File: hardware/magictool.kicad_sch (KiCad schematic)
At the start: 3 parts, among them J1 magicTool I/O, J2 RUN

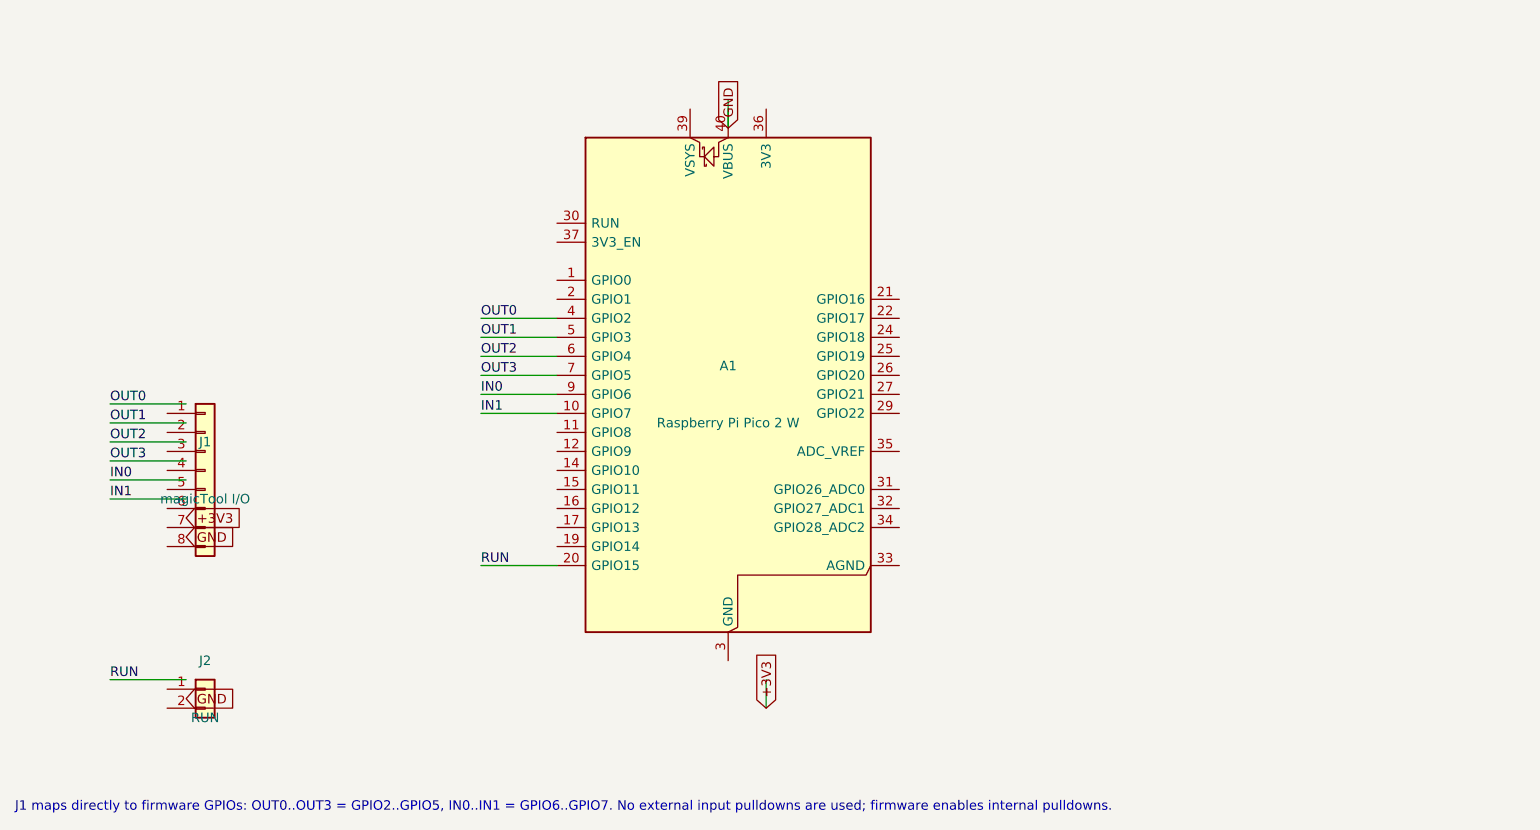
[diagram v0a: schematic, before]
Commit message: refactor(hardware): streamline schematic wiring and update labels
This commit enhances the Raspberry Pi Pico carrier schematic generation script by rerouting wires for improved readability, adjusting component positions for better alignment, and updating specific pin attributes to 'passive' where applicable. Additionally, it adds no-connect markers for unused Pico pins to prevent potential connection errors in the KiCad schematic. These changes aim to clarify signal routing and ensure consistency with standard schematic practices, thereby facilitating easier maintenance and modification of the design.
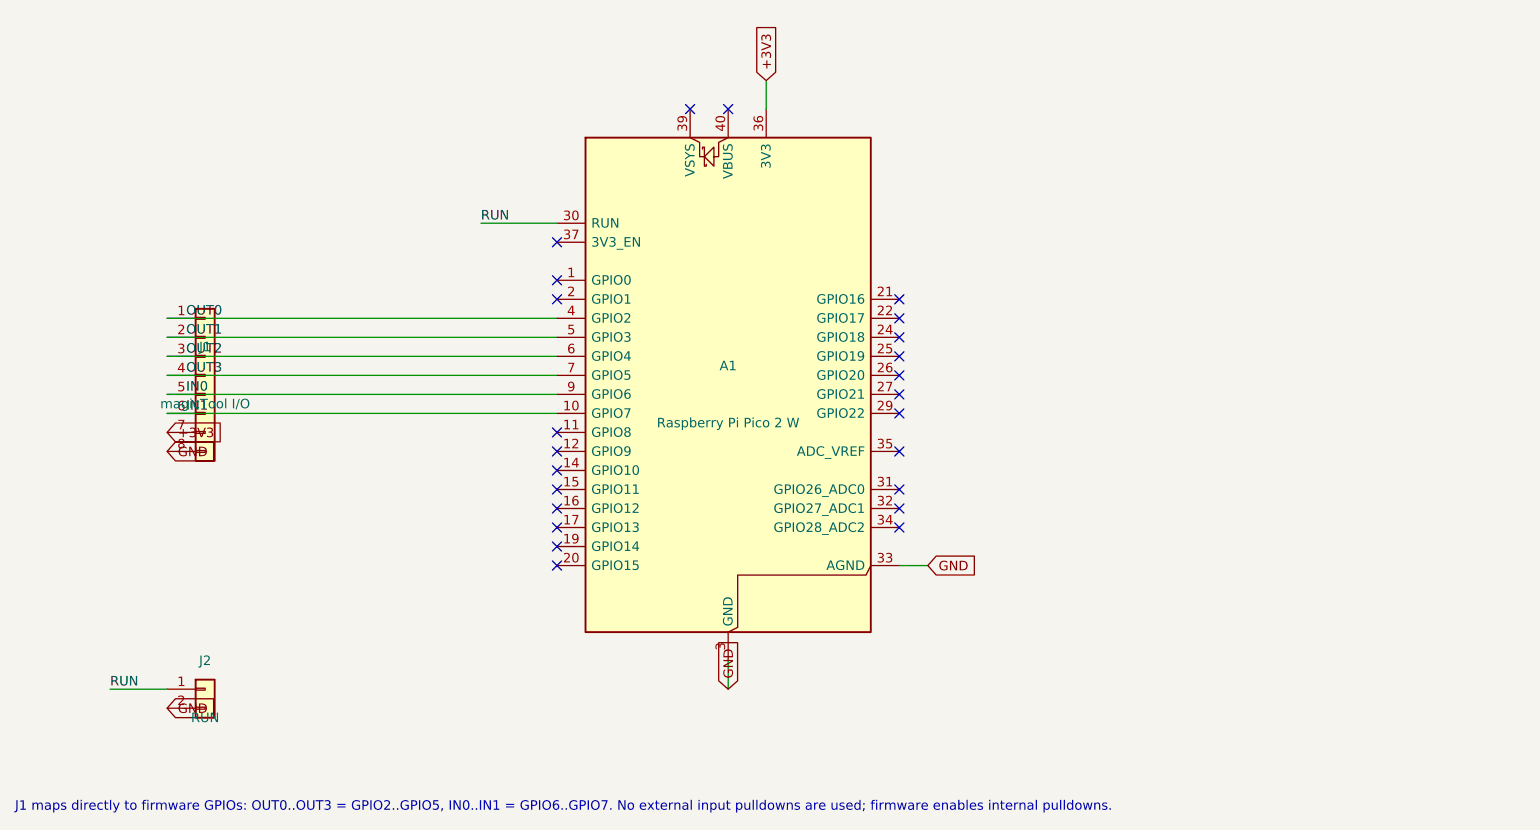
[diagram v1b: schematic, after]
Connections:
- net +3V3: now also A1.36 (3V3), J1.7 (Pin_7)
- net GND: now also A1.13 (GND), A1.18 (GND), A1.23 (GND), A1.28 (GND), A1.3 (GND), A1.33 (AGND), A1.38 (GND), A1.8 (GND), J1.8 (Pin_8), J2.2 (Pin_2)
- net IN0: now also J1.5 (Pin_5)
- net IN1: now also J1.6 (Pin_6)
- net OUT0: now also J1.1 (Pin_1)
- net OUT1: now also J1.2 (Pin_2)
- net OUT2: now also J1.3 (Pin_3)
- net OUT3: now also J1.4 (Pin_4)
- net RUN: now also A1.30 (RUN), J2.1 (Pin_1); no longer A1.20 (GPIO15)
- no-connect marks 0 -> 24
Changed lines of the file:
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@@
 	)
 	(wire
-		(pts (xy 97.79 78.74) (xy 87.63 78.74))
+		(pts (xy 45.72 78.74) (xy 97.79 78.74))
 		(stroke (width 0) (type default))
 	)
 	(label "OUT0"
-		(at 87.63 78.74 0)
-		(effects (font (size 1.27 1.27)) (justify left bottom))
-	)
-	(wire
-		(pts (xy 97.79 81.28) (xy 87.63 81.28))
+		(at 48.26 78.74 0)
+		(effects (font (size 1.27 1.27)) (justify left bottom))
+	)
+	(wire
+		(pts (xy 45.72 81.28) (xy 97.79 81.28))
 		(stroke (width 0) (type default))
 	)
 	(label "OUT1"
-		(at 87.63 81.28 0)
-		(effects (font (size 1.27 1.27)) (justify left bottom))
-	)
-	(wire
-		(pts (xy 97.79 83.82) (xy 87.63 83.82))
+		(at 48.26 81.28 0)
+		(effects (font (size 1.27 1.27)) (justify left bottom))
+	)
+	(wire
+		(pts (xy 45.72 83.82) (xy 97.79 83.82))
 		(stroke (width 0) (type default))
 	)
 	(label "OUT2"
-		(at 87.63 83.82 0)
-		(effects (font (size 1.27 1.27)) (justify left bottom))
-	)
-	(wire
-		(pts (xy 97.79 86.36) (xy 87.63 86.36))
+		(at 48.26 83.82 0)
+		(effects (font (size 1.27 1.27)) (justify left bottom))
+	)
+	(wire
+		(pts (xy 45.72 86.36) (xy 97.79 86.36))
 		(stroke (width 0) (type default))
 	)
 	(label "OUT3"
-		(at 87.63 86.36 0)
-		(effects (font (size 1.27 1.27)) (justify left bottom))
-	)
-	(wire
-		(pts (xy 97.79 88.9) (xy 87.63 88.9))
+		(at 48.26 86.36 0)
+		(effects (font (size 1.27 1.27)) (justify left bottom))
+	)
+	(wire
+		(pts (xy 45.72 88.9) (xy 97.79 88.9))
 		(stroke (width 0) (type default))
 	)
 	(label "IN0"
-		(at 87.63 88.9 0)
-		(effects (font (size 1.27 1.27)) (justify left bottom))
-	)
-	(wire
-		(pts (xy 97.79 91.44) (xy 87.63 91.44))
+		(at 48.26 88.9 0)
+		(effects (font (size 1.27 1.27)) (justify left bottom))
+	)
+	(wire
+		(pts (xy 45.72 91.44) (xy 97.79 91.44))
 		(stroke (width 0) (type default))
 	)
 	(label "IN1"
-		(at 87.63 91.44 0)
-		(effects (font (size 1.27 1.27)) (justify left bottom))
-	)
-	(wire
-		(pts (xy 48.26 90.17) (xy 38.1 90.17))
-		(stroke (width 0) (type default))
-	)
-	(label "OUT0"
-		(at 38.1 90.17 0)
-		(effects (font (size 1.27 1.27)) (justify left bottom))
-	)
-	(wire
-		(pts (xy 48.26 92.71) (xy 38.1 92.71))
-		(stroke (width 0) (type default))
-	)
-	(label "OUT1"
-		(at 38.1 92.71 0)
-		(effects (font (size 1.27 1.27)) (justify left bottom))
-	)
-	(wire
-		(pts (xy 48.26 95.25) (xy 38.1 95.25))
-		(stroke (width 0) (type default))
-	)
-	(label "OUT2"
-		(at 38.1 95.25 0)
-		(effects (font (size 1.27 1.27)) (justify left bottom))
-	)
-	(wire
-		(pts (xy 48.26 97.79) (xy 38.1 97.79))
-		(stroke (width 0) (type default))
-	)
-	(label "OUT3"
-		(at 38.1 97.79 0)
-		(effects (font (size 1.27 1.27)) (justify left bottom))
-	)
-	(wire
-		(pts (xy 48.26 100.33) (xy 38.1 100.33))
-		(stroke (width 0) (type default))
-	)
-	(label "IN0"
-		(at 38.1 100.33 0)
-		(effects (font (size 1.27 1.27)) (justify left bottom))
-	)
-	(wire
-		(pts (xy 48.26 102.87) (xy 38.1 102.87))
-		(stroke (width 0) (type default))
-	)
-	(label "IN1"
-		(at 38.1 102.87 0)
+		(at 48.26 91.44 0)
 		(effects (font (size 1.27 1.27)) (justify left bottom))
 	)
 	(global_label "+3V3"
 		(shape input)
-		(at 48.26 105.41 180)
-		(fields_autoplaced yes)
-		(effects (font (size 1.27 1.27)) (justify left))
-		(property "Intersheetrefs" "${INTERSHEET_REFS}" (at 48.26 105.41 0)
+		(at 45.72 93.98 180)
+		(fields_autoplaced yes)
+		(effects (font (size 1.27 1.27)) (justify left))
+		(property "Intersheetrefs" "${INTERSHEET_REFS}" (at 45.72 93.98 0)
 			(effects (font (size 1.27 1.27)) (hide yes))
 		)
@@
 	(global_label "GND"
 		(shape input)
-		(at 48.26 107.95 180)
-		(fields_autoplaced yes)
-		(effects (font (size 1.27 1.27)) (justify left))
-		(property "Intersheetrefs" "${INTERSHEET_REFS}" (at 48.26 107.95 0)
+		(at 45.72 96.52 180)
+		(fields_autoplaced yes)
+		(effects (font (size 1.27 1.27)) (justify left))
+		(property "Intersheetrefs" "${INTERSHEET_REFS}" (at 45.72 96.52 0)
 			(effects (font (size 1.27 1.27)) (hide yes))
 		)
@@
 	(global_label "+3V3"
 		(shape input)
-		(at 125.73 130.81 90)
-		(fields_autoplaced yes)
-		(effects (font (size 1.27 1.27)) (justify left))
-		(property "Intersheetrefs" "${INTERSHEET_REFS}" (at 125.73 130.81 0)
-			(effects (font (size 1.27 1.27)) (hide yes))
-		)
-	)
-	(wire
-		(pts (xy 125.73 127) (xy 125.73 130.81))
+		(at 125.73 46.99 90)
+		(fields_autoplaced yes)
+		(effects (font (size 1.27 1.27)) (justify left))
+		(property "Intersheetrefs" "${INTERSHEET_REFS}" (at 125.73 46.99 0)
+			(effects (font (size 1.27 1.27)) (hide yes))
+		)
+	)
+	(wire
+		(pts (xy 125.73 50.8) (xy 125.73 46.99))
 		(stroke (width 0) (type default))
 	)
 	(global_label "GND"
 		(shape input)
-		(at 120.65 53.34 270)
-		(fields_autoplaced yes)
-		(effects (font (size 1.27 1.27)) (justify left))
-		(property "Intersheetrefs" "${INTERSHEET_REFS}" (at 120.65 53.34 0)
-			(effects (font (size 1.27 1.27)) (hide yes))
-		)
-	)
-	(wire
-		(pts (xy 120.65 53.34) (xy 120.65 49.53))
-		(stroke (width 0) (type default))
-	)
-	(wire
-		(pts (xy 97.79 111.76) (xy 87.63 111.76))
+		(at 120.65 128.27 270)
+		(fields_autoplaced yes)
+		(effects (font (size 1.27 1.27)) (justify left))
+		(property "Intersheetrefs" "${INTERSHEET_REFS}" (at 120.65 128.27 0)
+			(effects (font (size 1.27 1.27)) (hide yes))
+		)
+	)
+	(wire
+		(pts (xy 120.65 124.46) (xy 120.65 128.27))
+		(stroke (width 0) (type default))
+	)
+	(global_label "GND"
+		(shape input)
+		(at 147.32 111.76 0)
+		(fields_autoplaced yes)
+		(effects (font (size 1.27 1.27)) (justify left))
+		(property "Intersheetrefs" "${INTERSHEET_REFS}" (at 147.32 111.76 0)
+			(effects (font (size 1.27 1.27)) (hide yes))
+		)
+	)
+	(wire
+		(pts (xy 143.51 111.76) (xy 147.32 111.76))
+		(stroke (width 0) (type default))
+	)
+	(wire
+		(pts (xy 97.79 66.04) (xy 87.63 66.04))
 		(stroke (width 0) (type default))
 	)
 	(label "RUN"
-		(at 87.63 111.76 0)
-		(effects (font (size 1.27 1.27)) (justify left bottom))
-	)
-	(wire
-		(pts (xy 48.26 127) (xy 38.1 127))
+		(at 87.63 66.04 0)
+		(effects (font (size 1.27 1.27)) (justify left bottom))
+	)
+	(wire
+		(pts (xy 45.72 128.27) (xy 38.1 128.27))
 		(stroke (width 0) (type default))
 	)
 	(label "RUN"
-		(at 38.1 127 0)
+		(at 38.1 128.27 0)
 		(effects (font (size 1.27 1.27)) (justify left bottom))
 	)
 	(global_label "GND"
 		(shape input)
-		(at 48.26 129.54 180)
-		(fields_autoplaced yes)
-		(effects (font (size 1.27 1.27)) (justify left))
-		(property "Intersheetrefs" "${INTERSHEET_REFS}" (at 48.26 129.54 0)
-			(effects (font (size 1.27 1.27)) (hide yes))
-		)
+		(at 45.72 130.81 180)
+		(fields_autoplaced yes)
+		(effects (font (size 1.27 1.27)) (justify left))
+		(property "Intersheetrefs" "${INTERSHEET_REFS}" (at 45.72 130.81 0)
+			(effects (font (size 1.27 1.27)) (hide yes))
+		)
+	)
+	(no_connect
+		(at 97.79 73.66)
+	)
+	(no_connect
+		(at 97.79 76.2)
+	)
+	(no_connect
+		(at 97.79 93.98)
+	)
+	(no_connect
+		(at 97.79 96.52)
+	)
+	(no_connect
+		(at 97.79 99.06)
+	)
+	(no_connect
+		(at 97.79 101.6)
+	)
+	(no_connect
+		(at 97.79 104.14)
+	)
+	(no_connect
+		(at 97.79 106.68)
+	)
+	(no_connect
+		(at 97.79 109.22)
+	)
+	(no_connect
+		(at 97.79 111.76)
+	)
+	(no_connect
+		(at 143.51 76.2)
+	)
+	(no_connect
+		(at 143.51 78.74)
+	)
+	(no_connect
+		(at 143.51 81.28)
+	)
+	(no_connect
+		(at 143.51 83.82)
+	)
+	(no_connect
+		(at 143.51 86.36)
+	)
+	(no_connect
+		(at 143.51 88.9)
+	)
+	(no_connect
+		(at 143.51 91.44)
+	)
+	(no_connect
+		(at 143.51 101.6)
+	)
+	(no_connect
+		(at 143.51 104.14)
+	)
+	(no_connect
+		(at 143.51 106.68)
+	)
+	(no_connect
+		(at 143.51 96.52)
+	)
+	(no_connect
+		(at 97.79 68.58)
+	)
+	(no_connect
+		(at 115.57 50.8)
+	)
+	(no_connect
+		(at 120.65 50.8)
 	)
 	(symbol
@@
 	(symbol
 		(lib_id "Connector_Generic:Conn_01x08")
-		(at 50.8 99.06 0)
+		(at 50.8 86.36 0)
 		(unit 1)
 		(exclude_from_sim no)
@@
 		(dnp no)
 		(property "Reference" "J1"
-			(at 50.8 95.25 0)
+			(at 50.8 82.55 0)
 			(effects (font (size 1.27 1.27)))
 		)
 		(property "Value" "magicTool I/O"
-			(at 50.8 102.87 0)
+			(at 50.8 90.17 0)
 			(effects (font (size 1.27 1.27)))
 		)
 		(property "Footprint" "Connector_PinHeader_2.54mm:PinHeader_1x08_P2.54mm_Vertical"
-			(at 50.8 99.06 0)
+			(at 50.8 86.36 0)
 			(effects (font (size 1.27 1.27)) (hide yes))
 		)
 		(property "Datasheet" "~"
-			(at 50.8 99.06 0)
+			(at 50.8 86.36 0)
 			(effects (font (size 1.27 1.27)) (hide yes))
 		)
 		(property "Description" ""
-			(at 50.8 99.06 0)
-			(effects (font (size 1.27 1.27)) (hide yes))
-		)
+			(at 50.8 86.36 0)
+			(effects (font (size 1.27 1.27)) (hide yes))
+		)
